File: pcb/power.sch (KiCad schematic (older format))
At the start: 16 parts, among them J2 Conn_01x03, U4 TSR_1-2433, U5 TSR_1-24150

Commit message: Version 2 PCB design (WIP)
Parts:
- removed J2: Conn_01x03, local:Multicomp_MC000049, symbol Conn_01x03
- removed TP41: TEST, Measurement_Points:Measurement_Point_Round-SMD-Pad_Small, symbol TEST
- added J6: Conn_01x02, Local:Multicomp_MC000048, symbol Conn_01x02
- C10: renamed from C13; footprint Capacitors_SMD:C_0805_HandSoldering -> Capacitors_SMD:C_1206_HandSoldering
- C11: renamed from C12; footprint Capacitors_SMD:C_0805_HandSoldering -> Capacitors_SMD:C_1206_HandSoldering
- renumbered R35 to R5, R36 to R6, R37 to R7, TP40 to TP5, TP42 to TP6, TP44 to TP7, TP43 to TP8
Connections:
- net labels removed: TP_EARTH
- wire segments 31 -> 30
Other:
- note added: "This is needed to stop KiCad's ERC complaining about\nthe 28V net not being driven. This warning occurs\nsince the pin that drives this net (J6 pin 2) is marked\nas passive (J6 is a standard library part so we can't\nchange that)."
- moved on the sheet: TP5, TP6
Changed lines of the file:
@@
 LIBS:valves
 LIBS:symbols
-LIBS:tape-punch-controller-cache
 EELAYER 25 0
 EELAYER END
@@
 $EndDescr
 $Comp
-L Conn_01x03 J2
-U 1 1 5A3BEC07
-P 3900 2600
-F 0 "J2" H 3900 2800 50  0000 C CNN
-F 1 "Conn_01x03" H 3900 2400 50  0000 C CNN
-F 2 "local:Multicomp_MC000049" H 3900 2600 50  0001 C CNN
-F 3 "" H 3900 2600 50  0001 C CNN
-	1    3900 2600
-	-1   0    0    1
-$EndComp
-$Comp
 L +28V #PWR019
 U 1 1 5A3BEEA9
-P 4900 2450
-F 0 "#PWR019" H 4900 2300 50  0001 C CNN
-F 1 "+28V" H 4900 2600 50  0000 C CNN
-F 2 "" H 5150 2500 50  0001 C CNN
-F 3 "" H 5150 2500 50  0001 C CNN
-	1    4900 2450
+P 4750 2500
+F 0 "#PWR019" H 4750 2350 50  0001 C CNN
+F 1 "+28V" H 4750 2650 50  0000 C CNN
+F 2 "" H 5000 2550 50  0001 C CNN
+F 3 "" H 5000 2550 50  0001 C CNN
+	1    4750 2500
 	1    0    0    -1
 $EndComp
@@
 L GND #PWR020
 U 1 1 5A3BEED9
-P 4900 2750
-F 0 "#PWR020" H 4900 2500 50  0001 C CNN
-F 1 "GND" H 4900 2600 50  0000 C CNN
-F 2 "" H 4900 2750 50  0001 C CNN
-F 3 "" H 4900 2750 50  0001 C CNN
-	1    4900 2750
-	1    0    0    -1
-$EndComp
-Text GLabel 5000 2600 2    60   UnSpc ~ 0
-TP_EARTH
-Wire Wire Line
-	4100 2500 4900 2500
-Wire Wire Line
-	4900 2500 4900 2450
-Wire Wire Line
-	4100 2600 5000 2600
-Wire Wire Line
-	4100 2700 4900 2700
-Wire Wire Line
-	4900 2700 4900 2750
+P 4750 2700
+F 0 "#PWR020" H 4750 2450 50  0001 C CNN
+F 1 "GND" H 4750 2550 50  0000 C CNN
+F 2 "" H 4750 2700 50  0001 C CNN
+F 3 "" H 4750 2700 50  0001 C CNN
+	1    4750 2700
+	1    0    0    -1
+$EndComp
+Wire Wire Line
+	4100 2550 4750 2550
+Wire Wire Line
+	4750 2550 4750 2500
+Wire Wire Line
+	4100 2650 4750 2650
+Wire Wire Line
+	4750 2650 4750 2700
 $Comp
 L TSR_1-2433 U4
@@
 $EndComp
 $Comp
-L C C12
+L C C11
 U 1 1 5A3ED752
 P 7750 4650
-F 0 "C12" H 7775 4750 50  0000 L CNN
+F 0 "C11" H 7775 4750 50  0000 L CNN
 F 1 "10u" H 7775 4550 50  0000 L CNN
-F 2 "Capacitors_SMD:C_0805_HandSoldering" H 7788 4500 50  0001 C CNN
+F 2 "Capacitors_SMD:C_1206_HandSoldering" H 7788 4500 50  0001 C CNN
 F 3 "" H 7750 4650 50  0001 C CNN
 	1    7750 4650
@@
 $EndComp
 $Comp
-L C C13
+L C C10
 U 1 1 5A3ED84B
 P 7750 2700
-F 0 "C13" H 7775 2800 50  0000 L CNN
+F 0 "C10" H 7775 2800 50  0000 L CNN
 F 1 "10u" H 7775 2600 50  0000 L CNN
-F 2 "Capacitors_SMD:C_0805_HandSoldering" H 7788 2550 50  0001 C CNN
+F 2 "Capacitors_SMD:C_1206_HandSoldering" H 7788 2550 50  0001 C CNN
 F 3 "" H 7750 2700 50  0001 C CNN
 	1    7750 2700
@@
 	7750 2900 7750 2850
 $Comp
-L R R35
+L R R5
 U 1 1 5A3EF81E
 P 3900 4250
-F 0 "R35" V 3980 4250 50  0000 C CNN
+F 0 "R5" V 3980 4250 50  0000 C CNN
 F 1 "1.8k" V 3900 4250 50  0000 C CNN
 F 2 "Resistors_SMD:R_1210_HandSoldering" V 3830 4250 50  0001 C CNN
@@
 $EndComp
 $Comp
-L R R36
+L R R6
 U 1 1 5A3EF881
 P 4400 4250
-F 0 "R36" V 4480 4250 50  0000 C CNN
+F 0 "R6" V 4480 4250 50  0000 C CNN
 F 1 "820" V 4400 4250 50  0000 C CNN
 F 2 "Resistors_SMD:R_1206_HandSoldering" V 4330 4250 50  0001 C CNN
@@
 $EndComp
 $Comp
-L R R37
+L R R7
 U 1 1 5A3EF8C2
 P 4900 4250
-F 0 "R37" V 4980 4250 50  0000 C CNN
+F 0 "R7" V 4980 4250 50  0000 C CNN
 F 1 "82" V 4900 4250 50  0000 C CNN
 F 2 "Resistors_SMD:R_0805_HandSoldering" V 4830 4250 50  0001 C CNN
@@
 	4900 4050 4900 4100
 $Comp
-L TEST TP40
+L TEST TP5
 U 1 1 5A43BC95
-P 4250 2450
-F 0 "TP40" H 4250 2750 50  0000 C BNN
-F 1 "TEST" H 4250 2700 50  0000 C CNN
-F 2 "Measurement_Points:Measurement_Point_Round-SMD-Pad_Small" H 4250 2450 50  0001 C CNN
-F 3 "" H 4250 2450 50  0001 C CNN
-	1    4250 2450
-	1    0    0    -1
-$EndComp
-$Comp
-L TEST TP41
-U 1 1 5A43BCE0
-P 4450 2450
-F 0 "TP41" H 4450 2750 50  0000 C BNN
-F 1 "TEST" H 4450 2700 50  0000 C CNN
-F 2 "Measurement_Points:Measurement_Point_Round-SMD-Pad_Small" H 4450 2450 50  0001 C CNN
-F 3 "" H 4450 2450 50  0001 C CNN
-	1    4450 2450
-	1    0    0    -1
-$EndComp
-$Comp
-L TEST TP42
+P 4250 2500
+F 0 "TP5" H 4250 2800 50  0000 C BNN
+F 1 "TEST" H 4250 2750 50  0000 C CNN
+F 2 "Measurement_Points:Measurement_Point_Round-SMD-Pad_Small" H 4250 2500 50  0001 C CNN
+F 3 "" H 4250 2500 50  0001 C CNN
+	1    4250 2500
+	1    0    0    -1
+$EndComp
+$Comp
+L TEST TP6
 U 1 1 5A43BD1B
-P 4650 2450
-F 0 "TP42" H 4650 2750 50  0000 C BNN
-F 1 "TEST" H 4650 2700 50  0000 C CNN
-F 2 "Measurement_Points:Measurement_Point_Round-SMD-Pad_Small" H 4650 2450 50  0001 C CNN
-F 3 "" H 4650 2450 50  0001 C CNN
-	1    4650 2450
-	1    0    0    -1
-$EndComp
-Wire Wire Line
-	4250 2450 4250 2500
-Connection ~ 4250 2500
-Wire Wire Line
-	4450 2450 4450 2600
-Connection ~ 4450 2600
-Wire Wire Line
-	4650 2450 4650 2700
-Connection ~ 4650 2700
-$Comp
-L TEST TP44
+P 4500 2500
+F 0 "TP6" H 4500 2800 50  0000 C BNN
+F 1 "TEST" H 4500 2750 50  0000 C CNN
+F 2 "Measurement_Points:Measurement_Point_Round-SMD-Pad_Small" H 4500 2500 50  0001 C CNN
+F 3 "" H 4500 2500 50  0001 C CNN
+	1    4500 2500
+	1    0    0    -1
+$EndComp
+Wire Wire Line
+	4250 2500 4250 2550
+Connection ~ 4250 2550
+Wire Wire Line
+	4500 2500 4500 2650
+Connection ~ 4500 2650
+$Comp
+L TEST TP7
 U 1 1 5A43CBD8
 P 7750 2450
-F 0 "TP44" H 7750 2750 50  0000 C BNN
+F 0 "TP7" H 7750 2750 50  0000 C BNN
 F 1 "TEST" H 7750 2700 50  0000 C CNN
 F 2 "Measurement_Points:Measurement_Point_Round-SMD-Pad_Small" H 7750 2450 50  0001 C CNN
@@
 	8050 2500 8050 2450
 $Comp
-L TEST TP43
+L TEST TP8
 U 1 1 5A43CE4F
 P 7750 4400
-F 0 "TP43" H 7750 4700 50  0000 C BNN
+F 0 "TP8" H 7750 4700 50  0000 C BNN
 F 1 "TEST" H 7750 4650 50  0000 C CNN
 F 2 "Measurement_Points:Measurement_Point_Round-SMD-Pad_Small" H 7750 4400 50  0001 C CNN
@@
 Wire Wire Line
 	8050 4450 8050 4400
-Text Notes 3850 1950 0    60   ~ 0
+Text Notes 3750 2050 0    60   ~ 0
 28V power input connector
 Text Notes 7000 2000 0    60   ~ 0
@@
 Text Notes 4200 3750 0    60   ~ 0
 Power LEDs
+$Comp
+L Conn_01x02 J6
+U 1 1 5A5A2D2F
+P 3900 2650
+F 0 "J6" H 3900 2750 50  0000 C CNN
+F 1 "Conn_01x02" H 3900 2450 50  0000 C CNN
+F 2 "Local:Multicomp_MC000048" H 3900 2650 50  0001 C CNN
+F 3 "" H 3900 2650 50  0001 C CNN
+	1    3900 2650
+	-1   0    0    1
+$EndComp
+$Comp
+L PWR_FLAG #FLG035
+U 1 1 5A5C13DD
+P 1750 6750
+F 0 "#FLG035" H 1750 6825 50  0001 C CNN
+F 1 "PWR_FLAG" H 1750 6900 50  0000 C CNN
+F 2 "" H 1750 6750 50  0001 C CNN
+F 3 "" H 1750 6750 50  0001 C CNN
+	1    1750 6750
+	-1   0    0    1
+$EndComp
+$Comp
+L +28V #PWR036
+U 1 1 5A5C1E08
+P 1750 6700
+F 0 "#PWR036" H 1750 6550 50  0001 C CNN
+F 1 "+28V" H 1750 6850 50  0000 C CNN
+F 2 "" H 2000 6750 50  0001 C CNN
+F 3 "" H 2000 6750 50  0001 C CNN
+	1    1750 6700
+	1    0    0    -1
+$EndComp
+Wire Wire Line
+	1750 6700 1750 6750
+Text Notes 2100 6950 0    60   ~ 0
+This is needed to stop KiCad's ERC complaining about\nthe 28V net not being driven. This warning occurs\nsince the pin that drives this net (J6 pin 2) is marked\nas passive (J6 is a standard library part so we can't\nchange that).
 $EndSCHEMATC

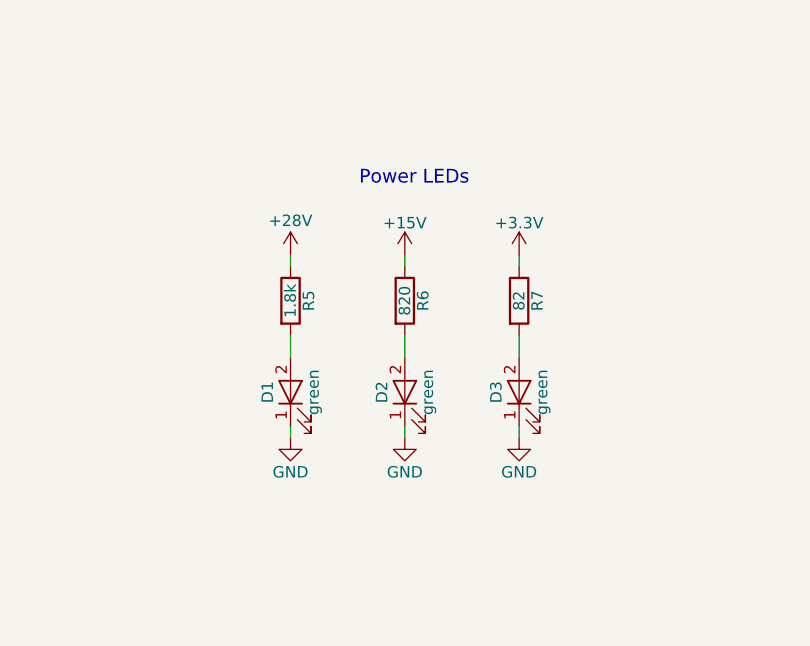
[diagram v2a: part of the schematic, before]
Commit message: pcb: remove power LEDs
We have test points and an external power LED, so they're pretty
redundant. They're also quite power hungry (the resistor for the
28V LED would dissipate about 300mW constantly), and removing them
reduces the number of different types of component used on the
board considerably.
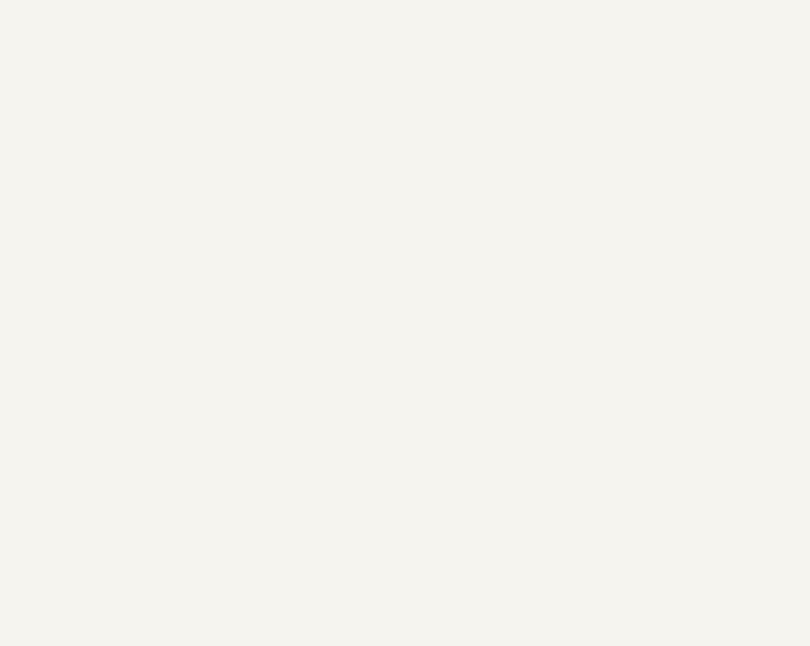
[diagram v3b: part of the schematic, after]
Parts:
- removed D1, D2, D3: green, LEDs:LED_0805_HandSoldering, symbol LED
- removed R5: 1.8k, Resistors_SMD:R_1210_HandSoldering, symbol R
- removed R6: 820, Resistors_SMD:R_1206_HandSoldering, symbol R
- removed R7: 82, Resistors_SMD:R_0805_HandSoldering, symbol R
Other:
- note removed: "Power LEDs"
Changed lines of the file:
@@
 	7750 2900 7750 2850
-$Comp
-L R R5
-U 1 1 5A3EF81E
-P 3900 4250
-F 0 "R5" V 3980 4250 50  0000 C CNN
-F 1 "1.8k" V 3900 4250 50  0000 C CNN
-F 2 "Resistors_SMD:R_1210_HandSoldering" V 3830 4250 50  0001 C CNN
-F 3 "" H 3900 4250 50  0001 C CNN
-	1    3900 4250
-	1    0    0    -1
-$EndComp
-$Comp
-L R R6
-U 1 1 5A3EF881
-P 4400 4250
-F 0 "R6" V 4480 4250 50  0000 C CNN
-F 1 "820" V 4400 4250 50  0000 C CNN
-F 2 "Resistors_SMD:R_1206_HandSoldering" V 4330 4250 50  0001 C CNN
-F 3 "" H 4400 4250 50  0001 C CNN
-	1    4400 4250
-	1    0    0    -1
-$EndComp
-$Comp
-L R R7
-U 1 1 5A3EF8C2
-P 4900 4250
-F 0 "R7" V 4980 4250 50  0000 C CNN
-F 1 "82" V 4900 4250 50  0000 C CNN
-F 2 "Resistors_SMD:R_0805_HandSoldering" V 4830 4250 50  0001 C CNN
-F 3 "" H 4900 4250 50  0001 C CNN
-	1    4900 4250
-	1    0    0    -1
-$EndComp
-$Comp
-L LED D1
-U 1 1 5A3EFAC9
-P 3900 4650
-F 0 "D1" H 3900 4750 50  0000 C CNN
-F 1 "green" H 3900 4550 50  0000 C CNN
-F 2 "LEDs:LED_0805_HandSoldering" H 3900 4650 50  0001 C CNN
-F 3 "" H 3900 4650 50  0001 C CNN
-	1    3900 4650
-	0    -1   -1   0
-$EndComp
-$Comp
-L LED D2
-U 1 1 5A3EFB40
-P 4400 4650
-F 0 "D2" H 4400 4750 50  0000 C CNN
-F 1 "green" H 4400 4550 50  0000 C CNN
-F 2 "LEDs:LED_0805_HandSoldering" H 4400 4650 50  0001 C CNN
-F 3 "" H 4400 4650 50  0001 C CNN
-	1    4400 4650
-	0    -1   -1   0
-$EndComp
-$Comp
-L LED D3
-U 1 1 5A3EFB83
-P 4900 4650
-F 0 "D3" H 4900 4750 50  0000 C CNN
-F 1 "green" H 4900 4550 50  0000 C CNN
-F 2 "LEDs:LED_0805_HandSoldering" H 4900 4650 50  0001 C CNN
-F 3 "" H 4900 4650 50  0001 C CNN
-	1    4900 4650
-	0    -1   -1   0
-$EndComp
-Wire Wire Line
-	3900 4400 3900 4500
-Wire Wire Line
-	4400 4400 4400 4500
-Wire Wire Line
-	4900 4400 4900 4500
-$Comp
-L GND #PWR030
-U 1 1 5A3F00B4
-P 3900 4850
-F 0 "#PWR030" H 3900 4600 50  0001 C CNN
-F 1 "GND" H 3900 4700 50  0000 C CNN
-F 2 "" H 3900 4850 50  0001 C CNN
-F 3 "" H 3900 4850 50  0001 C CNN
-	1    3900 4850
-	1    0    0    -1
-$EndComp
-$Comp
-L GND #PWR031
-U 1 1 5A3F033B
-P 4400 4850
-F 0 "#PWR031" H 4400 4600 50  0001 C CNN
-F 1 "GND" H 4400 4700 50  0000 C CNN
-F 2 "" H 4400 4850 50  0001 C CNN
-F 3 "" H 4400 4850 50  0001 C CNN
-	1    4400 4850
-	1    0    0    -1
-$EndComp
-$Comp
-L GND #PWR032
-U 1 1 5A3F0365
-P 4900 4850
-F 0 "#PWR032" H 4900 4600 50  0001 C CNN
-F 1 "GND" H 4900 4700 50  0000 C CNN
-F 2 "" H 4900 4850 50  0001 C CNN
-F 3 "" H 4900 4850 50  0001 C CNN
-	1    4900 4850
-	1    0    0    -1
-$EndComp
-Wire Wire Line
-	3900 4800 3900 4850
-Wire Wire Line
-	4400 4800 4400 4850
-Wire Wire Line
-	4900 4800 4900 4850
-$Comp
-L +28V #PWR033
-U 1 1 5A3F05A8
-P 3900 4050
-F 0 "#PWR033" H 3900 3900 50  0001 C CNN
-F 1 "+28V" H 3900 4200 50  0000 C CNN
-F 2 "" H 4150 4100 50  0001 C CNN
-F 3 "" H 4150 4100 50  0001 C CNN
-	1    3900 4050
-	1    0    0    -1
-$EndComp
-$Comp
-L +15V #PWR034
-U 1 1 5A3F05D2
-P 4400 4050
-F 0 "#PWR034" H 4400 3900 50  0001 C CNN
-F 1 "+15V" H 4400 4190 50  0000 C CNN
-F 2 "" H 4400 4050 50  0001 C CNN
-F 3 "" H 4400 4050 50  0001 C CNN
-	1    4400 4050
-	1    0    0    -1
-$EndComp
-$Comp
-L +3.3V #PWR035
-U 1 1 5A3F05FC
-P 4900 4050
-F 0 "#PWR035" H 4900 3900 50  0001 C CNN
-F 1 "+3.3V" H 4900 4190 50  0000 C CNN
-F 2 "" H 4900 4050 50  0001 C CNN
-F 3 "" H 4900 4050 50  0001 C CNN
-	1    4900 4050
-	1    0    0    -1
-$EndComp
-Wire Wire Line
-	3900 4050 3900 4100
-Wire Wire Line
-	4400 4050 4400 4100
-Wire Wire Line
-	4900 4050 4900 4100
 $Comp
 L TEST TP5
@@
 Text Notes 7100 3950 0    60   ~ 0
 15V regulator
-Text Notes 4200 3750 0    60   ~ 0
-Power LEDs
 $Comp
 L Conn_01x02 J6
